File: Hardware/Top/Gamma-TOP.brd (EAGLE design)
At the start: 0 parts

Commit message: First update to the Top board
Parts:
- added C10, C11: 300p, LinnesLab-Passives:C0603
- added C12: 10u, LinnesLab-Passives:C0805
- added C13, C15, C17, C18, C19: 2.2uF, LinnesLab-Passives:C0402
- added C14: 100n, LinnesLab-Passives:C0603
- added C16: 10uF, LinnesLab-Passives:C0603
- added C2, C5, C6, C7: 1u, LinnesLab-Passives:C0603
- added C20, C21: 4.7u, LinnesLab-Passives:C0603
- added C8, C9: (no value), LinnesLab-Passives:C0603
- added CHRG2: MCP73831, LinnesLab-Power:SOT23-5
- added CORTEX1: CORTEX_DEBUG_PTH, LinnesLab-Connectors:2X5-PTH-1.27MM
- added D1, D4, D5: (no value), LinnesLab-DiscreteSemi:USC
- added J2: (no value), LinnesLab-Connectors:1X02
- added L2: 10u, LinnesLab-Passives:L0603
- added LDO2: MIC5504, LinnesLab-Power:SOT23-5
- added LED3: RED, LinnesLab-LED:LED-0603
- added LED4: BLUE, LinnesLab-LED:LED-0603
- added R11: (no value), LinnesLab-Passives:R0603
- added R12, R13, R14, R15: 100k, LinnesLab-Passives:R0603
- added R3, R4: 1k, LinnesLab-Passives:R0603
- added R5, R6, R8, R9: 10k, LinnesLab-Passives:R0603
- added R7: 390k, LinnesLab-Passives:R0603
- added SD2: (no value), LinnesLab-Connectors:MICROSD
- added SW3, SW4: (no value), LinnesLab-Switches:BUTTON-GULLWING
- added SW6, SW7: SWITCH.MOM, LinnesLab-Switches:TACTILE_SWITCH_SMD_6.2MM_TALL
- added U2: NRF52832_MODULE_MDBT42, LinnesLab-Microcontrollers:BLE_MODULE_RAYTAC_MDBT42
- added U3: (no value), LinnesLab-Displays:UG-2864HSWEG01_0.96IN_NO-WRAPAROUND
- added U4: PCF8523, LinnesLab-Clocks:SO8
- added USB2: USB.MICRO-BIGGERPADS, LinnesLab-Connectors:USB-MICRO-01.BIGGERPADS
- added XTAL2: 32.768kHz, LinnesLab-Clocks:2-SMD.NOLEAD.2.0MMTO1.2MM
- added XTAL3: 32.7680kHz, LinnesLab-Clocks:2-SMD.NOLEAD.2.0MMTO1.2MM
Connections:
- new net 3.3V: C12.2, C17.2, C19.2, C2.1, C6.1, CORTEX1.1, D1.-, LDO2.5, R15.2, R5.2, R8.2, R9.2, SD2.4, U2.11, U3.6, U3.9, U4.8
- new net BATT: R13.1, R14.2
- new net CD1: SD2.CD1
- new net CD2: SD2.CD2
- new net CHRG.STAT: CHRG2.1, R12.1
- new net CS.OLED: U3.13
- new net DC.OLED: U3.15
- new net DFU: SW3.3, U2.34
- new net DTR: C14.1
- new net FRST: U2.38
- new net GND: C10.2, C11.2, C12.1, C16.1, C17.1, C18.1, C19.1, C2.2, C20.2, C21.1, C5.1, C6.2, C7.2, C8.1, C9.2, CHRG2.2, CORTEX1.3, CORTEX1.5, CORTEX1.7, CORTEX1.9, J2.1, LDO2.2, LED3.C, LED4.C, R11.1, R14.1, R15.1, R6.1, R7.2, SD2.6, SD2.MT1, SD2.MT2, SW3.1, SW4.3, SW6.B1, SW6.B2, SW7.B1, SW7.B2, U2.1, U2.12, U2.24, U2.39, U3.1, U3.10, U3.12, U3.29, U3.30, U3.8, U4.4, USB2.5
- new net LED1: R3.2, U2.31
- new net LED2: R4.2, U2.33
- new net MISO: SD2.7, U2.28
- new net MOSI: SD2.3, U2.27, U3.19
- new net N$1: R6.2, U3.11
- new net N$10: LED4.A, R4.1
- new net N$11: L2.1, U2.10
- new net N$12: C7.1, L2.2, U2.9
- new net N$13: C16.2, U3.28
- new net N$14: CORTEX1.8
- new net N$15: C18.2, U3.27
- new net N$17: CHRG2.5, R11.2
- new net N$19: U4.2, XTAL3.P$1
- new net N$2: R7.1, U3.26
- new net N$20: U4.1, XTAL3.P$2
- new net N$3: C13.2, U3.2
- new net N$4: C8.2, U2.13, XTAL2.P$1
- new net N$5: C13.1, U3.3
- new net N$6: C9.1, U2.14, XTAL2.P$2
- new net N$7: C15.2, U3.4
- new net N$8: C15.1, U3.5
- new net N$9: LED3.A, R3.1
- new net P0.09/NFC1: C11.1, U2.22
- new net P0.10/NFC2: C10.1, U2.23
- new net RESET: C14.2, CORTEX1.10, D1.+, R5.1, SW4.1, U2.35
- new net RESET.OLED: U3.14
- new net RXD: U2.21
- new net SCK: SD2.5, U2.26, U3.18
- new net SCL: R8.1, U2.3, U4.6
- new net SD.CS: SD2.2
- new net SDA: R9.1, U2.2, U4.5
- new net SW1: SW6.A1
- new net SW2: SW7.A1
- new net SWCLK: CORTEX1.4, U2.36
- new net SWDIO: CORTEX1.2, U2.37
- new net SWO: CORTEX1.6, U2.32
- new net TXD: U2.19
- new net USB+: USB2.3
- new net USB-: USB2.2
- new net VBATT: U4.3
- new net VIN: C21.2, C5.2, CHRG2.4, D4.-, D5.-, LDO2.1, LDO2.3, R12.2
- new net VLIPO: C20.1, CHRG2.3, D4.+, J2.2, R13.2
- new net V_USB: D5.+, USB2.1
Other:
- board outline added: 38 x 38 mm

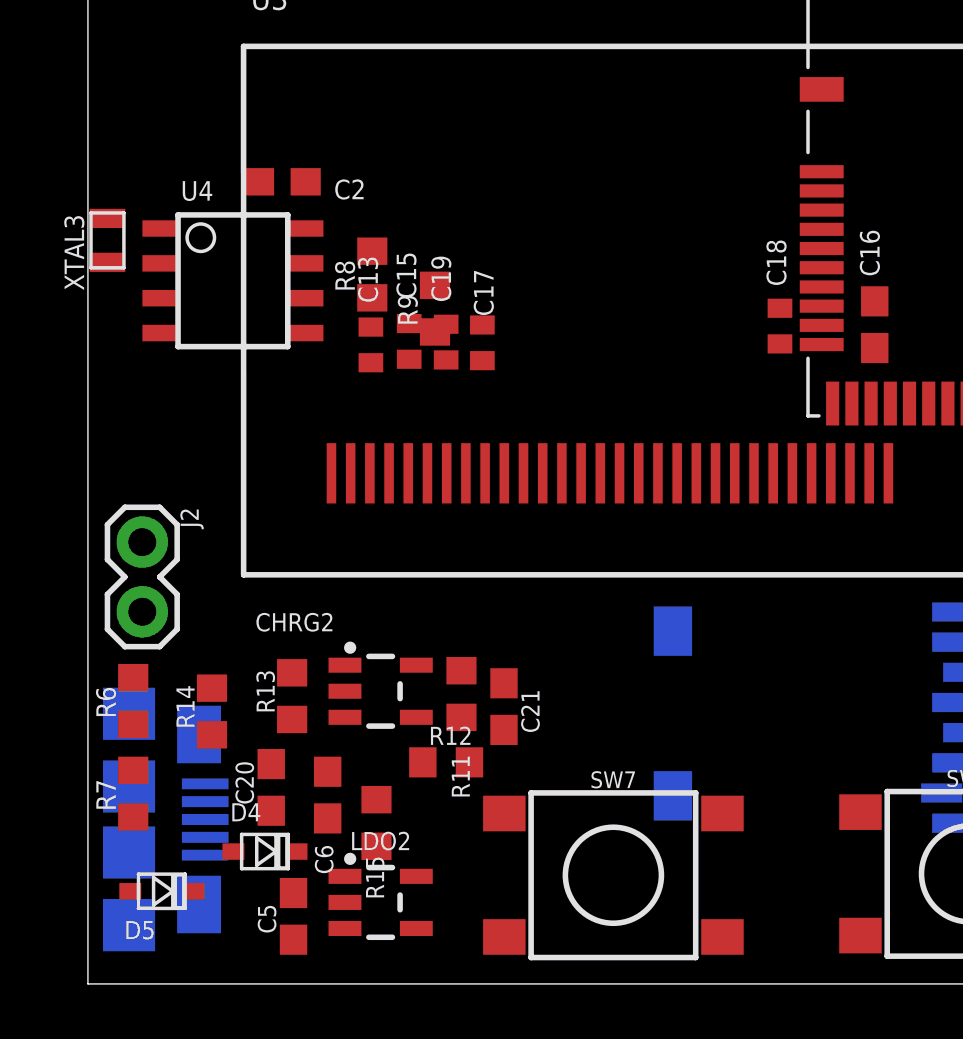
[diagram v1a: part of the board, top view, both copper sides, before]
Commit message: Fixed an overlap of two components
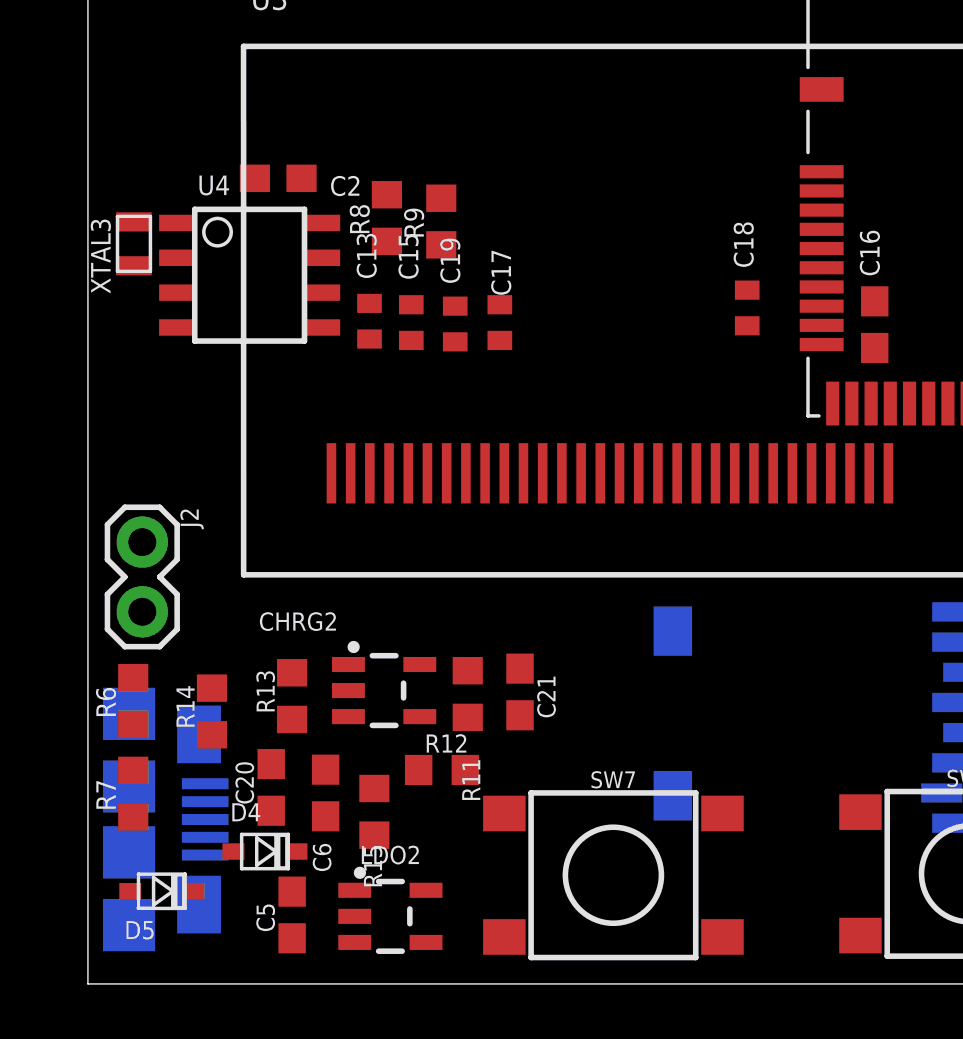
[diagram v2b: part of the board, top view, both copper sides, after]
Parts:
- moved R9 3.18 mm to (12.9, 27.8)
- moved R8 2.13 mm to (10.9, 27.9)
- moved C18 1.36 mm to (24.0, 24.6)
- moved XTAL3 0.97 mm to (1.68, 27.0)
- moved C17 0.97 mm to (15.0, 24.1)
- moved C13 0.87 mm to (10.3, 24.2)
- moved C21 0.79 mm to (15.7, 10.6)
- moved C19 0.74 mm to (13.4, 24.1)
- moved C15 0.69 mm to (11.8, 24.1)
- moved U4 0.64 mm to (5.89, 25.8)
- moved LDO2 0.62 mm to (11.0, 2.46)
- moved R15 0.41 mm to (10.4, 6.27)
- moved R12 0.32 mm to (12.9, 7.80)
- moved R11 0.23 mm to (13.8, 10.6)
- moved C2 0.20 mm to (6.93, 29.4)
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
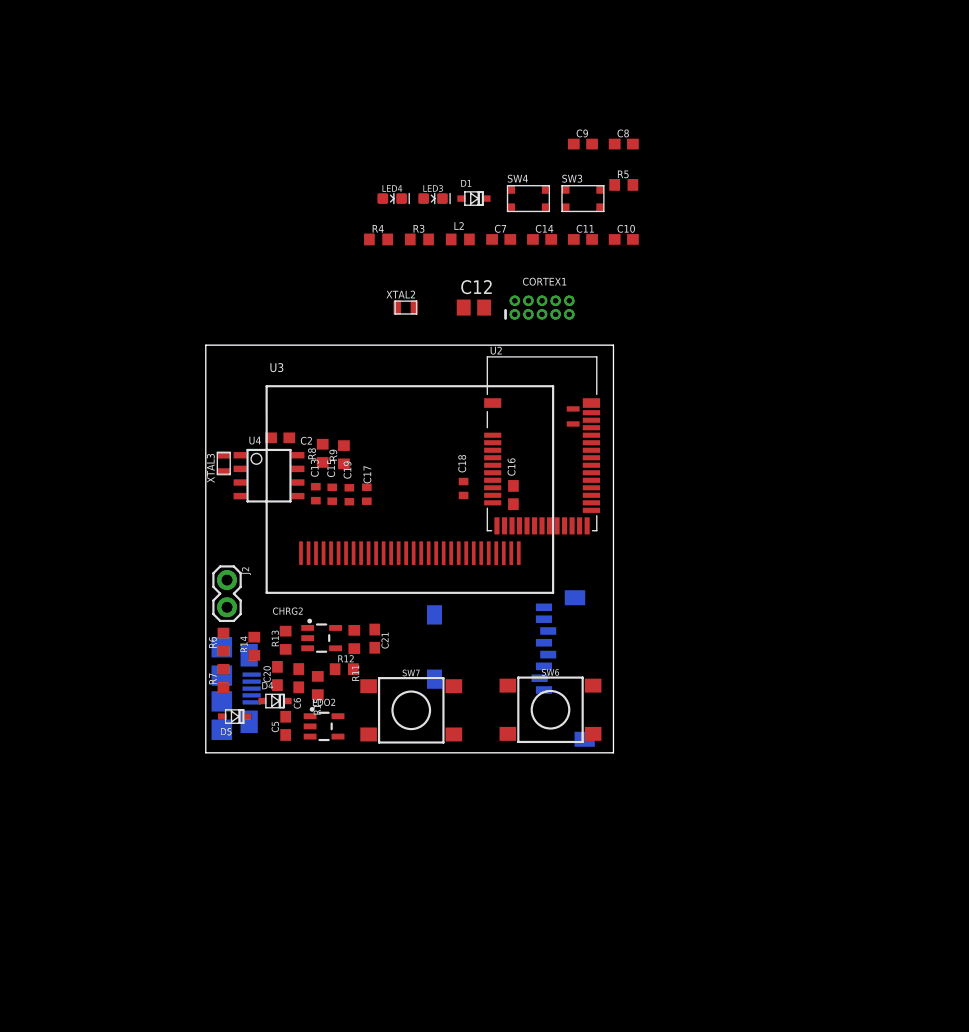
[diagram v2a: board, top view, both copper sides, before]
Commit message: Update to Top and Bottom Boards.  Top is not complete as of yet, and the bottom is ready for a check.  Routing not performed yet
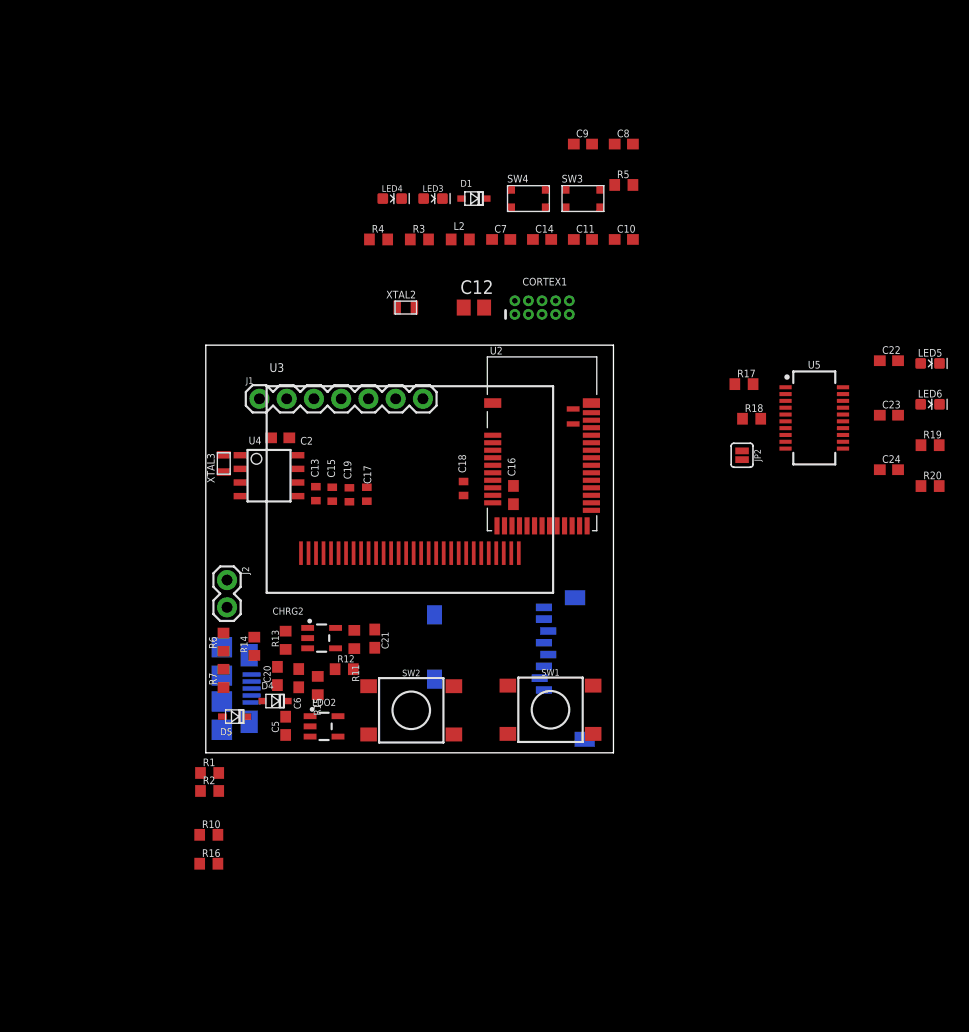
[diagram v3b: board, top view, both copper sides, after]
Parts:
- removed R8, R9: 10k, LinnesLab-Passives:R0603
- added C22: 100n, LinnesLab-Passives:C0603
- added C23, C24: 47p, LinnesLab-Passives:C0603
- added J1: (no value), LinnesLab-Connectors:1X07
- added JP2: (no value), LinnesLab-Switches:SMT-JUMPER_2_NO_SILK
- added LED5: RED, LinnesLab-LED:LED-0603
- added LED6: YELLOW, LinnesLab-LED:LED-0603
- added R1, R2: 0, LinnesLab-Passives:R0603
- added R10, R16: 10k, LinnesLab-Passives:R0603
- added R17, R18: 27, LinnesLab-Passives:R0603
- added R19, R20: 1k, LinnesLab-Passives:R0603
- added U5: FT231XS, LinnesLab-DigitalIC:SSOP20_L
- renumbered SW6 to SW1, SW7 to SW2
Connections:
- removed net BATT: R13.1, R14.2
- removed net CD1: SD2.CD1
- removed net CHRG.STAT: CHRG2.1, R12.1
- removed net CS.OLED: U3.13
- removed net DC.OLED: U3.15
- removed net RESET.OLED: U3.14
- removed net RXD: U2.21
- removed net SD.CS: SD2.2
- removed net SW1: SW1.A1
- removed net SW2: SW2.A1
- removed net TXD: U2.19
- new net !CTS: JP2.2, U5.9
- new net A4/BATT: R13.1, R14.2, U2.5
- new net A6/TIA: U2.7
- new net A7/PPG: U2.8
- new net D11/SW1: SW1.A1, U2.25
- new net D15/SW2: SW2.A1, U2.29
- new net D16/CS.OLED: U2.30, U3.13
- new net D27/CHRG.STATUS: CHRG2.1, R12.1, U2.4
- new net D29/LED.CTRL: U2.6
- new net D3/RESET.OLED: U2.16, U3.14
- new net D4/DC.OLED: U2.17, U3.15
- new net D5/CD1: SD2.CD1, U2.18
- new net D7/SD.CS: SD2.2, U2.20
- new net FT3V3: U5.13
- new net N$23: R17.2, U5.12
- new net N$24: R18.2, U5.11
- new net N$25: LED5.C, R19.2
- new net N$26: LED6.C, R20.2
- new net RXD.FT: R2.1, U5.4
- new net RXD.NRF: R1.2, U2.21
- new net RXLED: R19.1, U5.17
- new net TXD.FT: R1.1, U5.20
- new net TXD.NRF: R2.2, U2.19
- new net TXLED: R20.1, U5.10
- net 3.3V: now also C22.2, LED5.A, LED6.A, R10.1, R16.1, U5.14, U5.3; no longer R8.2, R9.2
- net DTR: now also U5.1
- net GND: now also C22.1, C23.2, C24.1, JP2.1, U5.16, U5.6
- net SCL: now also R10.2; no longer R8.1
- net SDA: now also R16.2; no longer R9.1
- net USB+: now also C23.1, R18.1
- net USB-: now also C24.2, R17.1
- net V_USB: now also U5.15

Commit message: Finished Take 004 up until deletion of NFC capacitors.  Board partially routed
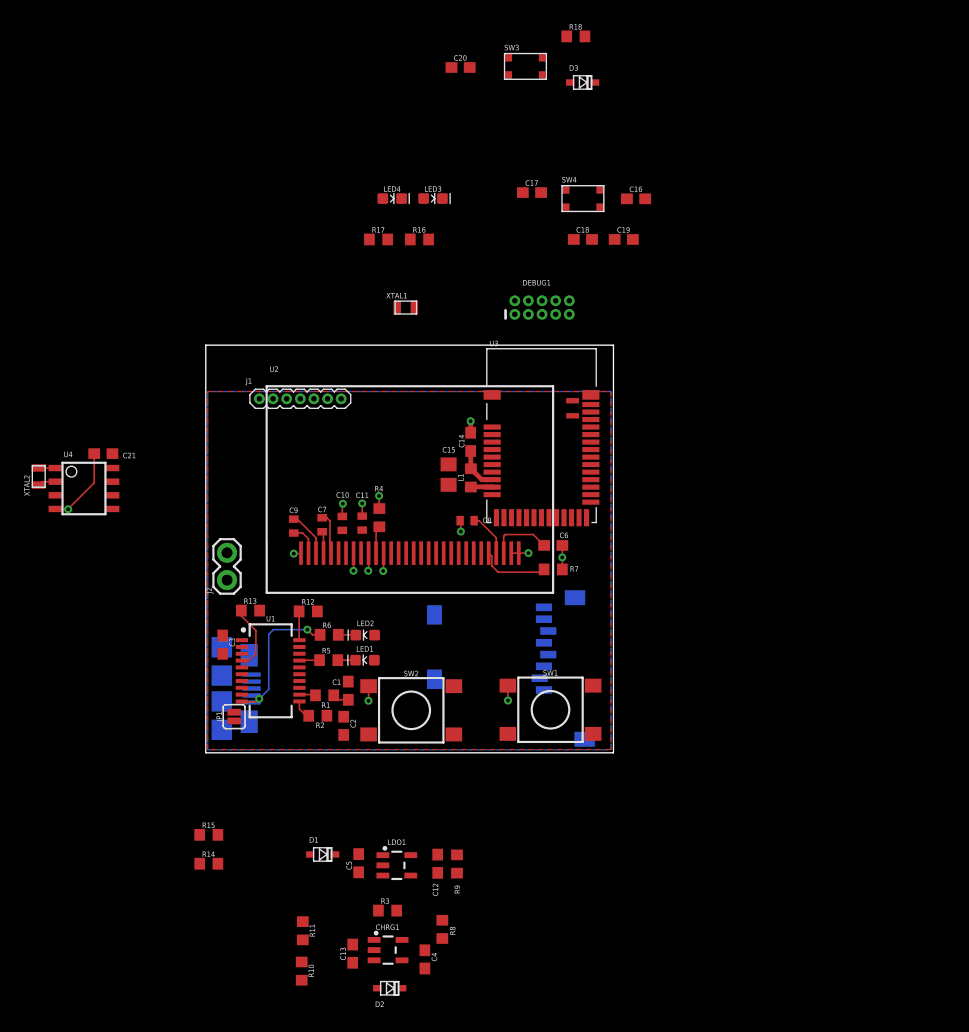
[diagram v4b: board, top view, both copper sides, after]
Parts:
- removed C22: 100n, LinnesLab-Passives:C0603
- removed C23, C24: 47p, LinnesLab-Passives:C0603
- removed CHRG2: MCP73831, LinnesLab-Power:SOT23-5
- removed D4, D5: (no value), LinnesLab-DiscreteSemi:USC
- removed JP2: (no value), LinnesLab-Switches:SMT-JUMPER_2_NO_SILK
- removed L2: 10u, LinnesLab-Passives:L0603
- removed LDO2: MIC5504, LinnesLab-Power:SOT23-5
- removed LED5: RED, LinnesLab-LED:LED-0603
- removed LED6: YELLOW, LinnesLab-LED:LED-0603
- removed R19, R20: 1k, LinnesLab-Passives:R0603
- removed U5: FT231XS, LinnesLab-DigitalIC:SSOP20_L
- removed XTAL3: 32.7680kHz, LinnesLab-Clocks:2-SMD.NOLEAD.2.0MMTO1.2MM
- added C1: 47p, LinnesLab-Passives:C0603
- added C3: 100n, LinnesLab-Passives:C0603
- added C4: 4.7u, LinnesLab-Passives:C0603
- added CHRG1: MCP73831, LinnesLab-Power:SOT23-5
- added D2, D3: (no value), LinnesLab-DiscreteSemi:USC
- added JP1: (no value), LinnesLab-Switches:SMT-JUMPER_2_NO_SILK
- added L1: 10u, LinnesLab-Passives:L0603
- added LDO1: MIC5504, LinnesLab-Power:SOT23-5
- added LED1: RED, LinnesLab-LED:LED-0603
- added LED2: YELLOW, LinnesLab-LED:LED-0603
- added R8: (no value), LinnesLab-Passives:R0603
- added R9: 100k, LinnesLab-Passives:R0603
- added U1: FT231XS, LinnesLab-DigitalIC:SSOP20_L
- added XTAL1: 32.768kHz, LinnesLab-Clocks:2-SMD.NOLEAD.2.0MMTO1.2MM
- C10, C11: value 300p -> 2.2uF; device LinnesLab-Passives:C0603 -> LinnesLab-Passives:C0402
- C12: value 10u -> 1u; device LinnesLab-Passives:C0805 -> LinnesLab-Passives:C0603
- C13: value 2.2uF -> 4.7u; device LinnesLab-Passives:C0402 -> LinnesLab-Passives:C0603
- C14: value 100n -> 1u
- C15: value 2.2uF -> 10u; device LinnesLab-Passives:C0402 -> LinnesLab-Passives:C0805
- C16: value 10uF -> (none)
- C17: value 2.2uF -> (none); device LinnesLab-Passives:C0402 -> LinnesLab-Passives:C0603
- C18, C19: value 2.2uF -> 300p; device LinnesLab-Passives:C0402 -> LinnesLab-Passives:C0603
- C2: value 1u -> 47p
- C20: value 4.7u -> 100n
- C21: value 4.7u -> 1u
- C6: value 1u -> 10uF
- C7: value 1u -> 2.2uF; device LinnesLab-Passives:C0603 -> LinnesLab-Passives:C0402
- C8, C9: value (none) -> 2.2uF; device LinnesLab-Passives:C0603 -> LinnesLab-Passives:C0402
- J1: device LinnesLab-Connectors:1X07 -> LinnesLab-Connectors:1X07_1.27MM
- R1, R2: value 0 -> 27
- R10: value 10k -> 100k
- R11: value (none) -> 100k
- R12, R13: value 100k -> 0
- R14, R15: value 100k -> 10k
- R16, R5, R6: value 10k -> 1k
- R17: value 27 -> 1k
- R18: value 27 -> 10k
- R3: value 1k -> 100k
- R4: value 1k -> 10k
- U2: value NRF52832_MODULE_MDBT42 -> (none); device LinnesLab-Microcontrollers:BLE_MODULE_RAYTAC_MDBT42 -> LinnesLab-Displays:UG-2864HSWEG01_0.96IN_NO-WRAPAROUND
- U3: value (none) -> NRF52832_MODULE_MDBT42; device LinnesLab-Displays:UG-2864HSWEG01_0.96IN_NO-WRAPAROUND -> LinnesLab-Microcontrollers:BLE_MODULE_RAYTAC_MDBT42
- XTAL2: value 32.768kHz -> 32.7680kHz
- moved D1 62.7 mm to (10.9, -9.47)
- moved R3 62.6 mm to (16.9, -14.7)
- moved R16 61.4 mm to (19.9, 47.9)
- moved C20 59.2 mm to (23.7, 63.9), turned to 0 degrees
- moved R5 52.1 mm to (11.5, 8.64)
- moved C12 52.0 mm to (21.6, -10.3), turned to 270 degrees
- moved C9 44.7 mm to (8.20, 21.1), turned to 270 degrees
- moved C13 43.0 mm to (13.7, -18.7)
- moved R18 39.2 mm to (34.5, 66.8)
- moved C8 38.0 mm to (24.4, 21.6)
- moved XTAL2 37.7 mm to (-15.6, 25.8), turned to 90 degrees
- moved C10 37.3 mm to (12.7, 21.4), turned to 270 degrees
- moved R17 36.6 mm to (16.1, 47.9)
- moved C19 34.9 mm to (39.0, 47.9), turned to 0 degrees
- moved C11 33.5 mm to (14.6, 21.4), turned to 270 degrees
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- renumbered CORTEX1 to DEBUG1, SD2 to SD1, USB2 to USB1
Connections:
- net !CTS: now also JP1.2, U1.9; no longer JP2.2, U5.9
- net 3.3V: now also C10.2, C11.2, C12.1, C15.2, C21.1, C3.2, D3.-, J1.4, LDO1.5, LED1.A, LED2.A, R14.1, R15.1, R18.2, R9.2, U1.14, U1.3, U2.6, U2.9, U3.11; no longer C12.2, C17.2, C19.2, C2.1, C22.2, C6.1, D1.-, LDO2.5, LED5.A, LED6.A, R10.1, R15.2, R16.1, R5.2, U2.11, U3.6, U3.9, U5.14, U5.3
- net A4/BATT: now also R10.1, R11.2, U3.5; no longer R13.1, R14.2, U2.5
- net A6/TIA: now also J1.6, U3.7; no longer U2.7
- net A7/PPG: now also J1.7, U3.8; no longer U2.8
- net D11/SW1: now also U3.25; no longer U2.25
- net D15/SW2: now also U3.29; no longer U2.29
- net D16/CS.OLED: now also U2.13, U3.30; no longer U2.30, U3.13
- net D27/CHRG.STATUS: now also CHRG1.1, R3.1, U3.4; no longer CHRG2.1, R12.1, U2.4
- net D29/LED.CTRL: now also J1.5, U3.6; no longer U2.6
- net D3/RESET.OLED: now also U2.14, U3.16; no longer U2.16, U3.14
- net D4/DC.OLED: now also U2.15, U3.17; no longer U2.17, U3.15
- net D5/CD1: now also U3.18; no longer U2.18
- net D7/SD.CS: now also U3.20; no longer U2.20
- net DFU: now also SW4.3, U3.34; no longer SW3.3, U2.34
- net DTR: now also C20.1, U1.1; no longer C14.1, U5.1
- net FRST: now also U3.38; no longer U2.38
- net FT3V3: now also U1.13; no longer U5.13
- net GND: now also C1.1, C10.1, C11.1, C12.2, C13.2, C14.2, C15.1, C17.2, C18.2, C19.2, C21.2, C3.1, C4.1, C6.1, CHRG1.2, J1.3, JP1.1, LDO1.2, R4.1, R8.1, R9.1, SW3.3, SW4.1, U1.16, U1.6, U2.10, U2.29, U2.30, U2.8, U3.24, U3.39; no longer C10.2, C11.2, C12.1, C17.1, C18.1, C19.1, C20.2, C21.1, C22.1, C23.2, C24.1, C6.2, C7.2, C9.2, CHRG2.2, JP2.1, LDO2.2, R14.1, R15.1, R6.1, SW3.1, SW4.3, U2.24, U2.39, U3.10, U3.29, U3.30, U3.8, U5.16, U5.6
- net LED1: now also R16.2, U3.31; no longer R3.2, U2.31
- net LED2: now also R17.2, U3.33; no longer R4.2, U2.33
- net MISO: now also U3.28; no longer U2.28
- net MOSI: now also U2.19, U3.27; no longer U2.27, U3.19
- net N$1: now also R4.2, U2.11; no longer R6.2, U3.11
- net N$10: now also R17.1; no longer R4.1
- net N$11: now also L1.1, U3.10; no longer L2.1, U2.10
- net N$12: now also C14.1, L1.2, U3.9; no longer C7.1, L2.2, U2.9
- net N$13: now also C6.2, U2.28; no longer C16.2, U3.28
- net N$15: now also C8.2, U2.27; no longer C18.2, U3.27
- net N$17: now also CHRG1.5, R8.2; no longer CHRG2.5, R11.2
- net N$19: now also XTAL2.P$1; no longer XTAL3.P$1
- net N$2: now also U2.26; no longer U3.26
- net N$20: now also XTAL2.P$2; no longer XTAL3.P$2
- net N$23: now also R1.2, U1.12; no longer R17.2, U5.12
- net N$24: now also R2.2, U1.11; no longer R18.2, U5.11
- net N$25: now also LED1.C, R5.2; no longer LED5.C, R19.2
- net N$26: now also LED2.C, R6.2; no longer LED6.C, R20.2
- net N$3: now also C9.2, U2.2; no longer C13.2, U3.2
- net N$4: now also C16.2, U3.13, XTAL1.P$1; no longer C8.2, U2.13, XTAL2.P$1
- net N$5: now also C9.1, U2.3; no longer C13.1, U3.3
- net N$6: now also C17.1, U3.14, XTAL1.P$2; no longer C9.1, U2.14, XTAL2.P$2
- net N$7: now also C7.2, U2.4; no longer C15.2, U3.4
- net N$8: now also C7.1, U2.5; no longer C15.1, U3.5
- net N$9: now also R16.1; no longer R3.1
- net P0.09/NFC1: now also C18.1, U3.22; no longer C11.1, U2.22
- net P0.10/NFC2: now also C19.1, U3.23; no longer C10.1, U2.23
- net RESET: now also C20.2, D3.+, R18.1, SW3.1, U3.35; no longer C14.2, D1.+, R5.1, SW4.1, U2.35
- net RXD.FT: now also R13.1, U1.4; no longer R2.1, U5.4
- net RXD.NRF: now also R12.2, U3.21; no longer R1.2, U2.21
- net RXLED: now also R5.1, U1.17; no longer R19.1, U5.17
- net SCK: now also U2.18, U3.26; no longer U2.26, U3.18
- net SCL: now also J1.2, R15.2, U3.3; no longer R10.2, U2.3
- net SDA: now also J1.1, R14.2, U3.2; no longer R16.2, U2.2
- net SWCLK: now also U3.36; no longer U2.36
- net SWDIO: now also U3.37; no longer U2.37
- net SWO: now also U3.32; no longer U2.32
- net TXD.FT: now also R12.1, U1.20; no longer R1.1, U5.20
- net TXD.NRF: now also R13.2, U3.19; no longer R2.2, U2.19
- net TXLED: now also R6.1, U1.10; no longer R20.1, U5.10
- net USB+: now also C2.1, R2.1; no longer C23.1, R18.1
- net USB-: now also C1.2, R1.1; no longer C24.2, R17.1
- net VIN: now also C4.2, CHRG1.4, D1.-, D2.-, LDO1.1, LDO1.3, R3.2; no longer C21.2, CHRG2.4, D4.-, D5.-, LDO2.1, LDO2.3, R12.2
- net VLIPO: now also C13.1, CHRG1.3, D1.+, R10.2; no longer C20.1, CHRG2.3, D4.+, R13.2
- net V_USB: now also D2.+, U1.15; no longer D5.+, U5.15
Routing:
- net GND: track 0.00 -> 25.4 mm, vias 0 -> 14
- net TXLED: track 0.00 -> 13.3 mm, vias 0 -> 2
- net N$2: track 0.00 -> 6.53 mm
- net RXD.FT: track 0.00 -> 6.15 mm
- net N$13: track 0.00 -> 5.83 mm
- net N$5: track 0.00 -> 4.22 mm
- net N$15: track 0.00 -> 4.16 mm
- net N$12: track 0.00 -> 4.05 mm
- net N$8: track 0.00 -> 3.89 mm
- net N$3: track 0.00 -> 2.94 mm
- net TXD.FT: track 0.00 -> 2.69 mm
- net N$1: track 0.00 -> 2.58 mm
- net N$7: track 0.00 -> 2.05 mm
- net N$11: track 0.00 -> 1.99 mm
- net RXLED: track 0.00 -> 1.90 mm
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- added copper zone on layer 1, net 3.3V
- added copper zone on layer 16, net GND
